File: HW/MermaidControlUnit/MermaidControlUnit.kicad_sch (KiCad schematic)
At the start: 0 parts

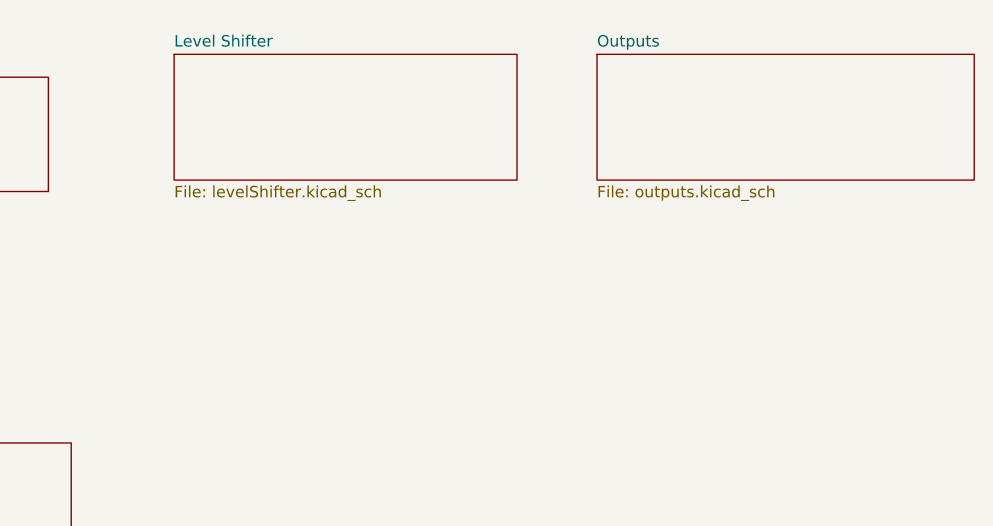
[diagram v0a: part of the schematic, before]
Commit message: folders reorganized, schematic progress
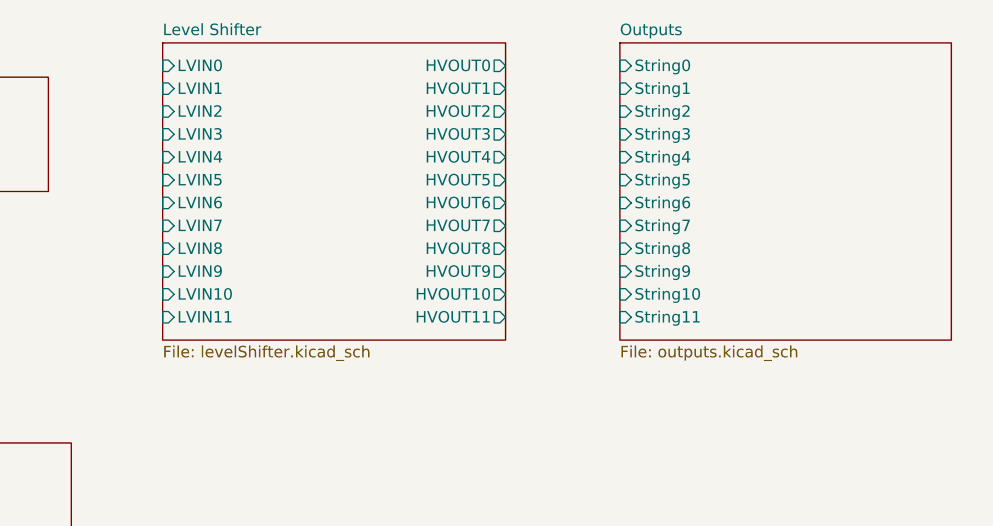
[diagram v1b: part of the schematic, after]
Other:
- sheet Level Shifter ports: added HVOUT0, HVOUT1, HVOUT10, HVOUT11, HVOUT2, HVOUT3, HVOUT4, HVOUT5, HVOUT6, HVOUT7, HVOUT8, HVOUT9, LVIN0, LVIN1, LVIN10, LVIN11, LVIN2, LVIN3, LVIN4, LVIN5, LVIN6, LVIN7, LVIN8, LVIN9; removed none
- sheet Outputs ports: added String0, String1, String10, String11, String2, String3, String4, String5, String6, String7, String8, String9; removed none
